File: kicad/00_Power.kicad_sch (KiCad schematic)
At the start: 0 parts

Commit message: Wire 00_Power: charger, LDO, USB-C, battery, status LEDs
Full BQ24075RGT 16-pin wiring (TS/CE/EN1/EN2/PGOOD/VSS/CHG/OUT/ILIM/
IN/TMR/SYSOFF/ISET per the locked pin table), AP2112K-3.3 LDO, USB-C
receptacle with CC pull-downs and USBLC6-2SC6 ESD protection, LiPo
battery + JST + voltage-sense divider, and CHG/PGOOD status LEDs.

Added PWR_FLAG symbols on the VBUS and GND nets to satisfy ERC --
both nets are only fed by passive-typed connector/battery pins, so
ERC has nothing it recognizes as a driver without an explicit flag.
Fixed USB-C SHIELD (tied to GND) and SBU1/SBU2 (no-connect, unused
in a USB2.0-only design) along the way.

Sheet ERC-clean except three cross-sheet nets (USB_D-, USB_D+,
CHG_CE) that are still single-ended pending 01_MCU.

Co-Authored-By: Claude Sonnet 5 <noreply@anthropic.com>
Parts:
- added BT1: Battery_Cell, symbol Device:Battery_Cell
- added C1, C4, C5: 1uF, Transformer_THT:Transformer_Breve_TEZ-22x24, symbol Device:C_Small
- added C2, C3: 4.7uF, Transformer_THT:Transformer_Breve_TEZ-22x24, symbol Device:C_Small
- added D2: PGOOD_LED, Package_TO_SOT_SMD:SOT-23-5, symbol Device:LED
- added D3: CHG_LED, Package_TO_SOT_SMD:SOT-23-5, symbol Device:LED
- added J1: USB_C_Receptacle_USB2.0_16P, Package_TO_SOT_SMD:SOT-23-6, symbol Connector:USB_C_Receptacle_USB2.0_16P
- added J2: LiPo, Connector_JST:JST_PH_B2B-PH-K_1x02_P2.00mm_Vertical, symbol Connector_Generic:Conn_01x02
- added R1, R2: 5.1k, Package_TO_SOT_SMD:SOT-23-6, symbol Device:R_Small
- added R3: 10k, Package_TO_SOT_SMD:SOT-23-6, symbol Device:R_Small
- added R4, R5: 1.5k, Package_TO_SOT_SMD:SOT-23-6, symbol Device:R_Small
- added R6: 1.18k, Package_TO_SOT_SMD:SOT-23-6, symbol Device:R_Small
- added R7: 1.78k 1%, Package_TO_SOT_SMD:SOT-23-6, symbol Device:R_Small
- added R8, R9: 100k, Package_TO_SOT_SMD:SOT-23-6, symbol Device:R_Small
- added U1: USBLC6-2SC6, Package_TO_SOT_SMD:SOT-23-6, symbol Power_Protection:USBLC6-2SC6
- added U2: BQ24075RGT, Package_DFN_QFN:VQFN-16-1EP_3x3mm_P0.5mm_EP1.6x1.6mm, symbol Battery_Management:BQ24075RGT
- added U3: AP2112K-3.3, Package_TO_SOT_SMD:SOT-23-5, symbol Regulator_Linear:AP2112K-3.3
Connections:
- new net: J1.B5 (CC2), R2.1
- new net: R5.1, U2.9 (~{CHG})
- new net: D3.1 (K), R5.2
- new net: R3.1, U2.1 (TS)
- new net: R6.2, U2.12 (ILIM)
- new net: R7.2, U2.16 (ISET)
- new net: R4.1, U2.7 (~{PGOOD})
- new net: J1.A7 (D-), J1.B7 (D-), U1.1 (I/O1)
- new net: J1.A6 (D+), J1.B6 (D+), U1.3 (I/O2)
- new net: D2.1 (K), R4.2
- new net: J1.A5 (CC1), R1.1
- new net +3V3: C4.1, U3.5 (VOUT)
- new net BATT: BT1.1 (+), C2.1, J2.1 (Pin_1), R8.1, U2.2 (BAT), U2.3 (BAT)
- new net CHG_CE: U2.4 (~{CE})
- new net GND: BT1.2 (-), C1.2, C2.2, C3.2, C4.2, C5.2, J1.A1 (GND), J1.A12 (GND), J1.B1 (GND), J1.B12 (GND), J1.SH (SHIELD), J2.2 (Pin_2), R1.2, R2.2, R3.2, R6.1, R7.1, R9.2, U1.2 (GND), U2.15 (SYSOFF), U2.17 (VSS), U2.6 (EN1), U2.8 (VSS), U3.2 (GND)
- new net USB_D+: U1.4 (I/O2)
- new net USB_D-: U1.6 (I/O1)
- new net USB_VBUS: C1.1, J1.A4 (VBUS), J1.A9 (VBUS), J1.B4 (VBUS), J1.B9 (VBUS), U1.5 (VBUS), U2.13 (IN)
- new net VBAT_OUT: C3.1, C5.1, D2.2 (A), D3.2 (A), U2.10 (OUT), U2.11 (OUT), U2.5 (EN2), U3.1 (VIN), U3.3 (EN)
- new net VBAT_SENSE: R8.2, R9.1
- no-connect marks 0 -> 3

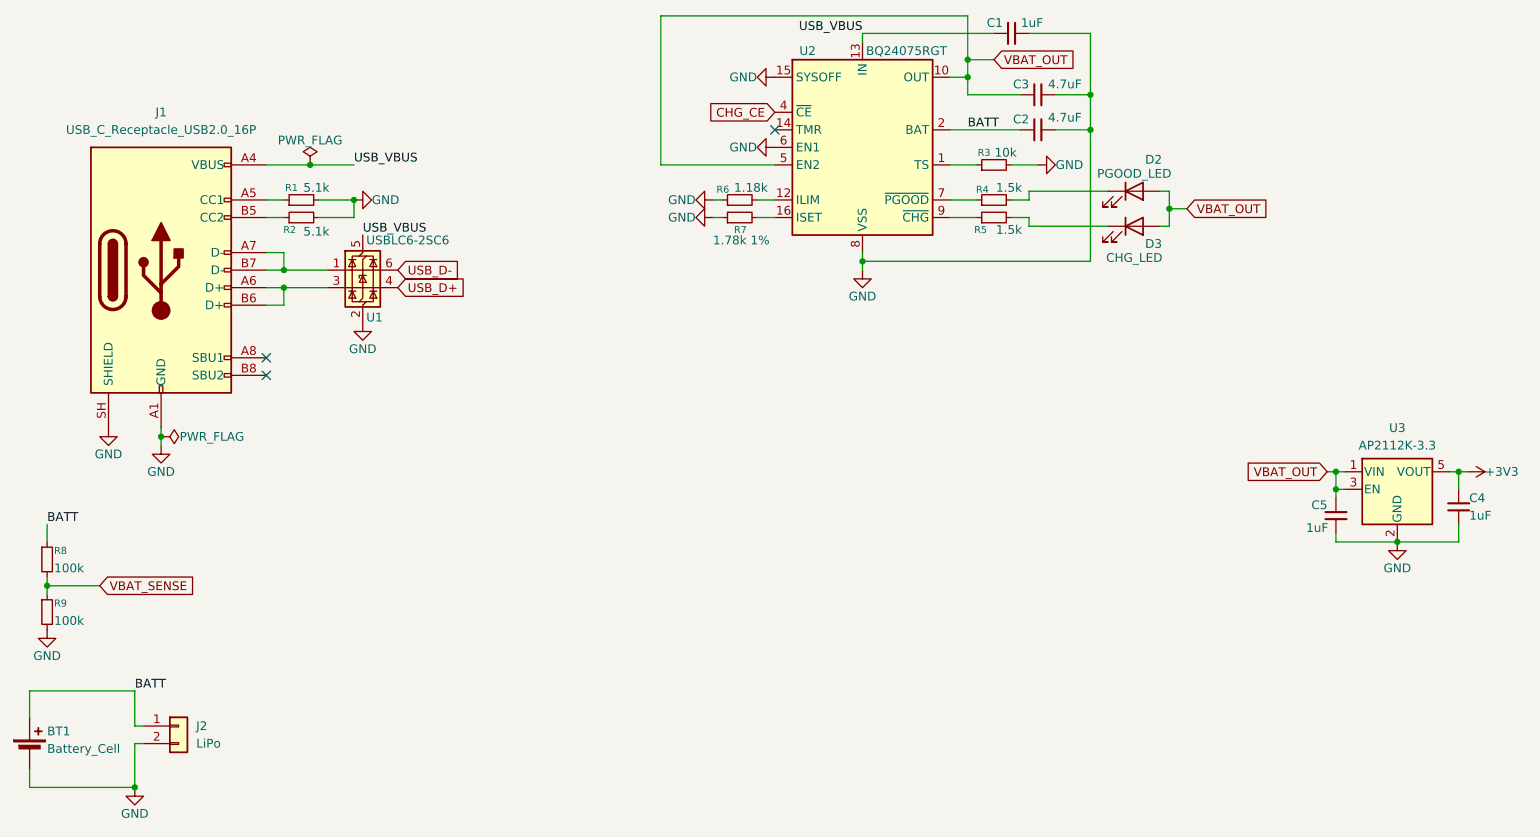
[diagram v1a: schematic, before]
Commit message: Wire 01_MCU: ESP32-S3, boot/reset/power buttons, all GPIO labels
ESP32-S3-WROOM-1 with VDD3P3 bulk cap, three button circuits
(EN/reset with debounce cap, IO0/boot, IO2/power - all 10k pull-up
to 3V3), USB_D-/USB_D+ tied to 00_Power's global labels, and a
global label on every remaining assigned GPIO matching the locked
pin table (LCD_*, I2C0_*, I2C1_*, I2S_*, TOF_*, TTP223_*, UART_*,
WS2812_*, MOTOR_PWM, LDR_ADC, CHG_CE, VBAT_SENSE). IO45/IO46 left
untouched (strapping). Added a 3-pin header (3V3/GND/GPIO48_SPARE)
for the one free GPIO, and two TestPoint pads (3V3, VBAT_OUT) on
00_Power for quick multimeter access.

ERC: 0 errors, 27 warnings -- all "label connected to only one pin"
on the peripheral-facing global labels waiting on their own sheets
(02_Display through 08_Misc_IO), exactly the expected set with no
unexplained entries.

Co-Authored-By: Claude Sonnet 5 <noreply@anthropic.com>
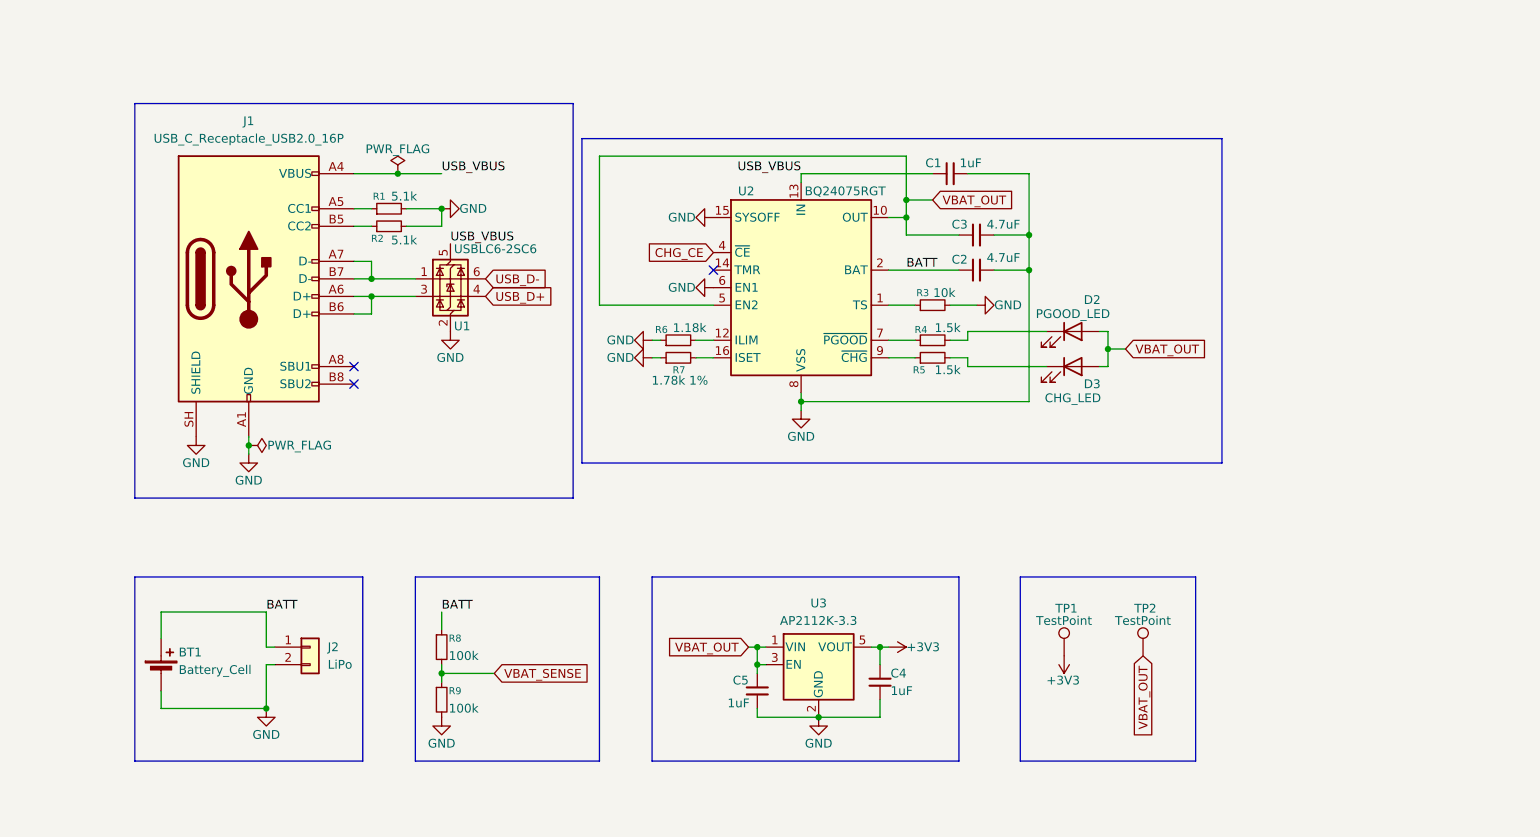
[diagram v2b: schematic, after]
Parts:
- added TP1, TP2: TestPoint, symbol Connector:TestPoint
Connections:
- net +3V3: now also TP1.1
- net VBAT_OUT: now also TP2.1
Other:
- moved on the sheet: BT1, C1, C2, C3, C4, C5, D2, D3, J1, J2, R1, R2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

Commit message: Footprint atamaları düzeltildi, satın alım listesi eklendi
- R/C/LED 0805, USB-C USB4110, tactile switch PTS645SM43SMTR92
- C6 47uF 1206, D5 BAT54 yerine SS14 (SMA)
- J8 JST ve TestPoint footprint'leri atandı
- purchase-list.md eklendi, BOM/plan/notlar güncellendi

Co-Authored-By: Claude Sonnet 5.5 <noreply@anthropic.com>
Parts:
- C1, C2, C3, C4, C5: footprint Transformer_THT:Transformer_Breve_TEZ-22x24 -> Capacitor_SMD:C_0805_2012Metric
- D2, D3: footprint Package_TO_SOT_SMD:SOT-23-5 -> LED_SMD:LED_0805_2012Metric
- J1: footprint Package_TO_SOT_SMD:SOT-23-6 -> Connector_USB:USB_C_Receptacle_GCT_USB4110
- R1, R2, R3, R4, R5, R6, R7, R8, R9: footprint Package_TO_SOT_SMD:SOT-23-6 -> Resistor_SMD:R_0805_2012Metric
- TP1, TP2: footprint (none) -> TestPoint:TestPoint_Pad_D1.5mm
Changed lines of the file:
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@@
 			)
 		)
-		(property "Footprint" "Package_TO_SOT_SMD:SOT-23-6"
+		(property "Footprint" "Resistor_SMD:R_0805_2012Metric"
 			(at 73.66 54.61 0)
 			(hide yes)
@@
 			)
 		)
-		(property "Footprint" ""
+		(property "Footprint" "TestPoint:TestPoint_Pad_D1.5mm"
 			(at 187.96 116.84 0)
 			(hide yes)
@@
 			)
 		)
-		(property "Footprint" "Package_TO_SOT_SMD:SOT-23-6"
+		(property "Footprint" "Resistor_SMD:R_0805_2012Metric"
 			(at 152.4 73.66 0)
 			(hide yes)
@@
 			)
 		)
-		(property "Footprint" "Package_TO_SOT_SMD:SOT-23-6"
+		(property "Footprint" "Resistor_SMD:R_0805_2012Metric"
 			(at 81.28 123.19 0)
 			(hide yes)
@@
 			)
 		)
-		(property "Footprint" ""
+		(property "Footprint" "TestPoint:TestPoint_Pad_D1.5mm"
 			(at 176.53 116.84 0)
 			(hide yes)
@@
 			)
 		)
-		(property "Footprint" "Transformer_THT:Transformer_Breve_TEZ-22x24"
+		(property "Footprint" "Capacitor_SMD:C_0805_2012Metric"
 			(at 158.75 60.96 0)
 			(hide yes)
@@
 			)
 		)
-		(property "Footprint" "Transformer_THT:Transformer_Breve_TEZ-22x24"
+		(property "Footprint" "Capacitor_SMD:C_0805_2012Metric"
 			(at 144.78 120.65 0)
 			(hide yes)
@@
 			)
 		)
-		(property "Footprint" "Package_TO_SOT_SMD:SOT-23-6"
+		(property "Footprint" "Resistor_SMD:R_0805_2012Metric"
 			(at 152.4 66.04 0)
 			(hide yes)
@@
 			)
 		)
-		(property "Footprint" "Package_TO_SOT_SMD:SOT-23-5"
+		(property "Footprint" "LED_SMD:LED_0805_2012Metric"
 			(at 172.72 74.93 0)
 			(hide yes)
@@
 			)
 		)
-		(property "Footprint" "Package_TO_SOT_SMD:SOT-23-6"
+		(property "Footprint" "Resistor_SMD:R_0805_2012Metric"
 			(at 152.4 71.12 0)
 			(hide yes)
@@
 			)
 		)
-		(property "Footprint" "Package_TO_SOT_SMD:SOT-23-6"
+		(property "Footprint" "Connector_USB:USB_C_Receptacle_GCT_USB4110"
 			(at 57.15 62.23 0)
 			(hide yes)
@@
 			)
 		)
-		(property "Footprint" "Package_TO_SOT_SMD:SOT-23-6"
+		(property "Footprint" "Resistor_SMD:R_0805_2012Metric"
 			(at 73.66 52.07 0)
 			(hide yes)
@@
 			)
 		)
-		(property "Footprint" "Transformer_THT:Transformer_Breve_TEZ-22x24"
+		(property "Footprint" "Capacitor_SMD:C_0805_2012Metric"
 			(at 154.94 46.99 0)
 			(hide yes)
@@
 			)
 		)
-		(property "Footprint" "Package_TO_SOT_SMD:SOT-23-6"
+		(property "Footprint" "Resistor_SMD:R_0805_2012Metric"
 			(at 115.57 73.66 0)
 			(hide yes)
@@
 			)
 		)
-		(property "Footprint" "Transformer_THT:Transformer_Breve_TEZ-22x24"
+		(property "Footprint" "Capacitor_SMD:C_0805_2012Metric"
 			(at 158.75 55.88 0)
 			(hide yes)
@@
 			)
 		)
-		(property "Footprint" "Package_TO_SOT_SMD:SOT-23-5"
+		(property "Footprint" "LED_SMD:LED_0805_2012Metric"
 			(at 172.72 69.85 0)
 			(hide yes)
@@
 			)
 		)
-		(property "Footprint" "Package_TO_SOT_SMD:SOT-23-6"
+		(property "Footprint" "Resistor_SMD:R_0805_2012Metric"
 			(at 115.57 71.12 0)
 			(hide yes)
@@
 			)
 		)
-		(property "Footprint" "Transformer_THT:Transformer_Breve_TEZ-22x24"
+		(property "Footprint" "Capacitor_SMD:C_0805_2012Metric"
 			(at 127 121.92 0)
 			(hide yes)
@@
 			)
 		)
-		(property "Footprint" "Package_TO_SOT_SMD:SOT-23-6"
+		(property "Footprint" "Resistor_SMD:R_0805_2012Metric"
 			(at 81.28 115.57 0)
 			(hide yes)
